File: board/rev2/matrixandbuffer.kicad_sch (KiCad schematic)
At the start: 4 parts, among them J5 Conn_02x08_Counter_Clockwise, SW2 MS-22D28-G020, U15 74HCT245

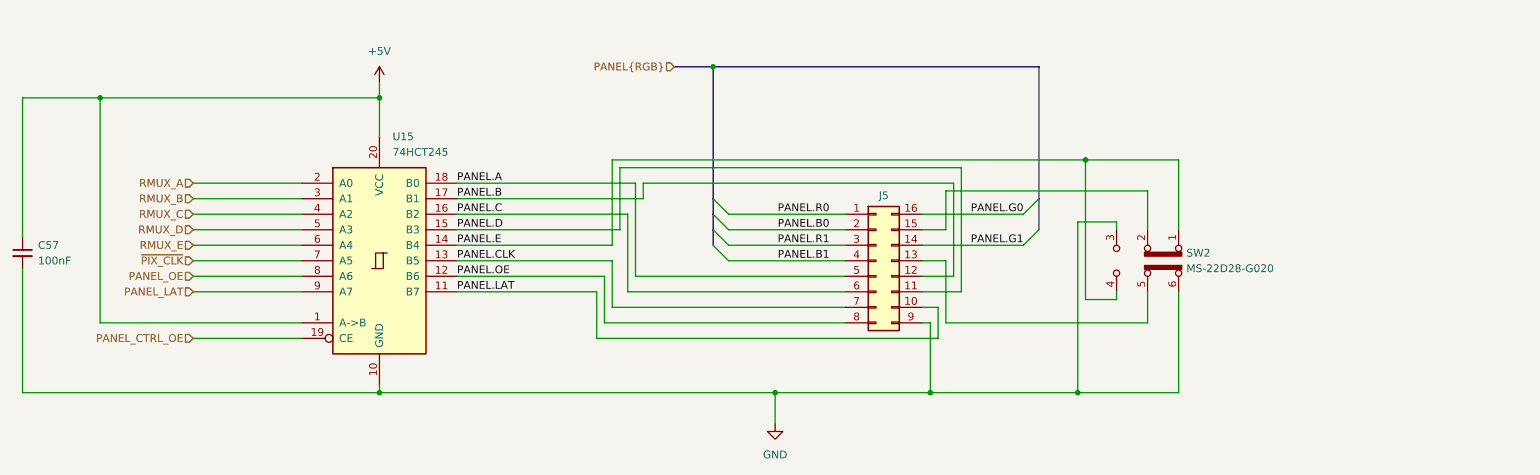
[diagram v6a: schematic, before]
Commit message: Really finish rev2 board schematic
- fix some more footprints
  - move to real SD card holder, for example
- repair part numbers
- add LCSC part refs to everything
- add even more caps to the 3.3V reg output
  - really should use an LDO but meh it should be fine

total BOM cost for 5 of them is apparently 160 CAD, or like 32 dollars
each (don't think that includes the feeder fees tho)
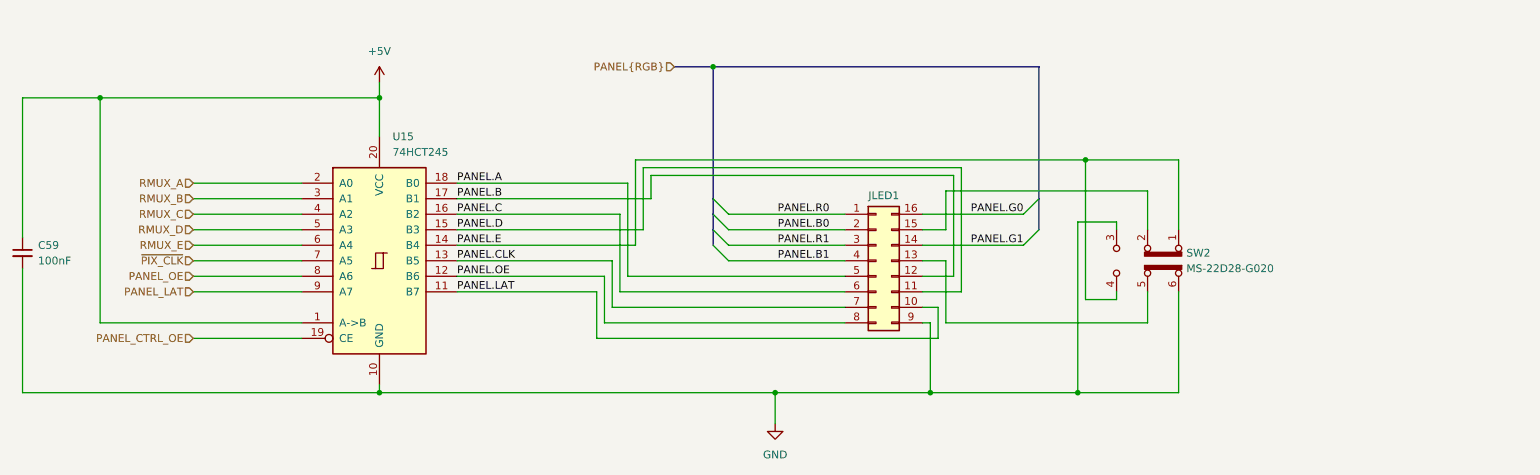
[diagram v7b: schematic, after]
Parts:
- C59: renamed from C57; LCSC (none) -> C307331
- SW2: LCSC (none) -> C963205
- U15: footprint Package_SO:TSSOP-20-1EP_4.4x6.5mm_P0.65mm_EP2.15x3.35mm -> Package_SO:TSSOP-20_4.4x6.5mm_P0.65mm; LCSC (none) -> C5980; Part 74HCT245 -> 74HCT245PW,118
- renumbered J5 to JLED1
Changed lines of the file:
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@@
 	(wire
 		(pts
-			(xy 138.43 91.44) (xy 138.43 104.14)
-		)
-		(stroke
-			(width 0)
-			(type default)
-		)
-	)
-	(wire
-		(pts
-			(xy 110.49 86.36) (xy 139.7 86.36)
+			(xy 137.16 91.44) (xy 137.16 104.14)
+		)
+		(stroke
+			(width 0)
+			(type default)
+		)
+	)
+	(wire
+		(pts
+			(xy 110.49 86.36) (xy 138.43 86.36)
 		)
 		(stroke
@@
 	(wire
 		(pts
-			(xy 139.7 101.6) (xy 173.99 101.6)
-		)
-		(stroke
-			(width 0)
-			(type default)
-		)
-	)
-	(wire
-		(pts
-			(xy 137.16 83.82) (xy 193.04 83.82)
+			(xy 138.43 101.6) (xy 173.99 101.6)
+		)
+		(stroke
+			(width 0)
+			(type default)
+		)
+	)
+	(wire
+		(pts
+			(xy 140.97 83.82) (xy 193.04 83.82)
 		)
 		(stroke
@@
 	(wire
 		(pts
-			(xy 137.16 93.98) (xy 137.16 83.82)
-		)
-		(stroke
-			(width 0)
-			(type default)
-		)
-	)
-	(wire
-		(pts
-			(xy 138.43 104.14) (xy 173.99 104.14)
+			(xy 140.97 93.98) (xy 140.97 83.82)
+		)
+		(stroke
+			(width 0)
+			(type default)
+		)
+	)
+	(wire
+		(pts
+			(xy 137.16 104.14) (xy 173.99 104.14)
 		)
 		(stroke
@@
 	(wire
 		(pts
-			(xy 110.49 93.98) (xy 137.16 93.98)
+			(xy 110.49 93.98) (xy 140.97 93.98)
 		)
 		(stroke
@@
 	(wire
 		(pts
-			(xy 135.89 82.55) (xy 213.36 82.55)
-		)
-		(stroke
-			(width 0)
-			(type default)
-		)
-	)
-	(wire
-		(pts
-			(xy 140.97 88.9) (xy 140.97 86.36)
+			(xy 139.7 82.55) (xy 213.36 82.55)
+		)
+		(stroke
+			(width 0)
+			(type default)
+		)
+	)
+	(wire
+		(pts
+			(xy 142.24 88.9) (xy 142.24 85.09)
 		)
 		(stroke
@@
 	(wire
 		(pts
-			(xy 140.97 86.36) (xy 191.77 86.36)
+			(xy 142.24 85.09) (xy 191.77 85.09)
 		)
 		(stroke
@@
 	(wire
 		(pts
-			(xy 110.49 91.44) (xy 138.43 91.44)
-		)
-		(stroke
-			(width 0)
-			(type default)
-		)
-	)
-	(wire
-		(pts
-			(xy 139.7 86.36) (xy 139.7 101.6)
+			(xy 110.49 91.44) (xy 137.16 91.44)
+		)
+		(stroke
+			(width 0)
+			(type default)
+		)
+	)
+	(wire
+		(pts
+			(xy 138.43 86.36) (xy 138.43 101.6)
 		)
 		(stroke
@@
 	(wire
 		(pts
-			(xy 191.77 86.36) (xy 191.77 101.6)
+			(xy 191.77 85.09) (xy 191.77 101.6)
 		)
 		(stroke
@@
 	(wire
 		(pts
-			(xy 110.49 96.52) (xy 135.89 96.52)
+			(xy 110.49 96.52) (xy 139.7 96.52)
 		)
 		(stroke
@@
 	(wire
 		(pts
-			(xy 135.89 96.52) (xy 135.89 82.55)
+			(xy 139.7 96.52) (xy 139.7 82.55)
 		)
 		(stroke
@@
 	(wire
 		(pts
-			(xy 110.49 88.9) (xy 140.97 88.9)
+			(xy 110.49 88.9) (xy 142.24 88.9)
 		)
 		(stroke
@@
 			)
 		)
-		(property "Footprint" "Package_SO:TSSOP-20-1EP_4.4x6.5mm_P0.65mm_EP2.15x3.35mm"
+		(property "Footprint" "Package_SO:TSSOP-20_4.4x6.5mm_P0.65mm"
 			(at 97.79 99.06 0)
 			(effects
@@
 			)
 		)
-		(property "Part" "74HCT245"
+		(property "Part" "74HCT245PW,118"
+			(at 97.79 99.06 0)
+			(effects
+				(font
+					(size 1.27 1.27)
+				)
+				(hide yes)
+			)
+		)
+		(property "LCSC" "C5980"
 			(at 97.79 99.06 0)
 			(effects
@@
 		(dnp no)
 		(fields_autoplaced yes)
-		(property "Reference" "C57"
+		(property "Reference" "C59"
 			(at 41.91 96.5262 0)
 			(effects
@@
 		)
 		(property "Part" "CL05B104KB54PNC"
+			(at 39.37 97.79 0)
+			(effects
+				(font
+					(size 1.27 1.27)
+				)
+				(hide yes)
+			)
+		)
+		(property "LCSC" "C307331 "
 			(at 39.37 97.79 0)
 			(effects
@@
 			(project "mainboard"
 				(path "/32eb05c7-b4a6-42f3-8fb3-43453631100f/b5a611d3-6308-4792-ad5f-d479afbae4ce"
-					(reference "C57")
+					(reference "C59")
 					(unit 1)
 				)
 				(path "/32eb05c7-b4a6-42f3-8fb3-43453631100f/e7e17249-2796-40aa-8cf6-7a1737723276"
-					(reference "C58")
+					(reference "C60")
 					(unit 1)
 				)
@@
 		(dnp no)
 		(fields_autoplaced yes)
-		(property "Reference" "#PWR045"
+		(property "Reference" "#PWR046"
 			(at 97.79 73.66 0)
 			(effects
@@
 			(project "mainboard"
 				(path "/32eb05c7-b4a6-42f3-8fb3-43453631100f/b5a611d3-6308-4792-ad5f-d479afbae4ce"
-					(reference "#PWR045")
+					(reference "#PWR046")
 					(unit 1)
 				)
 				(path "/32eb05c7-b4a6-42f3-8fb3-43453631100f/e7e17249-2796-40aa-8cf6-7a1737723276"
-					(reference "#PWR047")
+					(reference "#PWR048")
 					(unit 1)
 				)
@@
 			)
 		)
+		(property "LCSC" "C963205"
+			(at 223.52 99.06 90)
+			(effects
+				(font
+					(size 1.27 1.27)
+				)
+				(hide yes)
+			)
+		)
 		(pin "5"
 		)
@@
 		(on_board yes)
 		(dnp no)
-		(property "Reference" "J5"
+		(property "Reference" "JLED1"
 			(at 180.34 88.392 0)
 			(effects
@@
 					(size 1.27 1.27)
 					(color 255 255 194 1)
+				)
+				(hide yes)
+			)
+		)
+		(property "LCSC" ""
+			(at 179.07 99.06 0)
+			(effects
+				(font
+					(size 1.27 1.27)
 				)
 				(hide yes)
@@
 			(project "mainboard"
 				(path "/32eb05c7-b4a6-42f3-8fb3-43453631100f/b5a611d3-6308-4792-ad5f-d479afbae4ce"
-					(reference "J5")
+					(reference "JLED1")
 					(unit 1)
 				)
 				(path "/32eb05c7-b4a6-42f3-8fb3-43453631100f/e7e17249-2796-40aa-8cf6-7a1737723276"
-					(reference "J6")
+					(reference "JLED2")
 					(unit 1)
 				)
@@
 		(dnp no)
 		(fields_autoplaced yes)
-		(property "Reference" "#PWR046"
+		(property "Reference" "#PWR047"
 			(at 162.56 132.08 0)
 			(effects
@@
 			(project "mainboard"
 				(path "/32eb05c7-b4a6-42f3-8fb3-43453631100f/b5a611d3-6308-4792-ad5f-d479afbae4ce"
-					(reference "#PWR046")
+					(reference "#PWR047")
 					(unit 1)
 				)
 				(path "/32eb05c7-b4a6-42f3-8fb3-43453631100f/e7e17249-2796-40aa-8cf6-7a1737723276"
-					(reference "#PWR048")
+					(reference "#PWR049")
 					(unit 1)
 				)

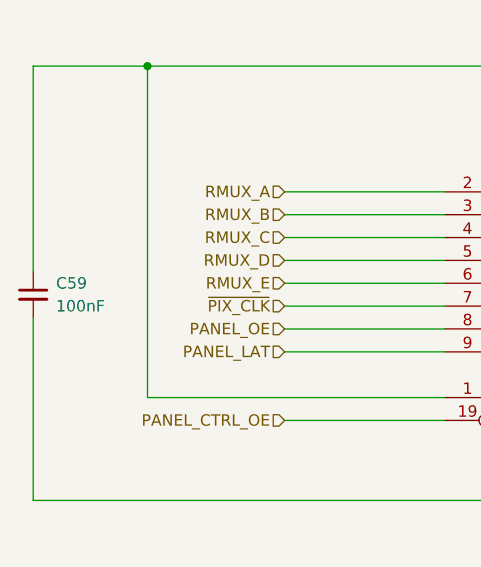
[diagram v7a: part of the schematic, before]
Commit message: Start board
add a few extra bypass caps too, and swap some pins on the USB mux

i forgot to add a bypass cap on the tpd6s so that also needs to happen

truly 63 capacitors is not enough
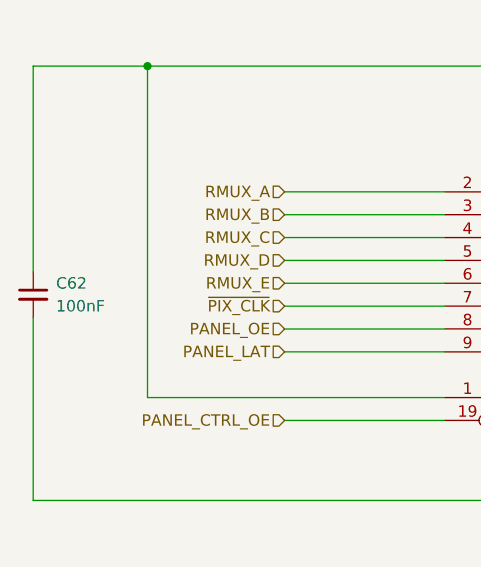
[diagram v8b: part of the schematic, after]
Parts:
- renumbered C59 to C62
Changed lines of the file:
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@@
 		(dnp no)
 		(fields_autoplaced yes)
-		(property "Reference" "C59"
+		(property "Reference" "C62"
 			(at 41.91 96.5262 0)
 			(effects
@@
 			(project "mainboard"
 				(path "/32eb05c7-b4a6-42f3-8fb3-43453631100f/b5a611d3-6308-4792-ad5f-d479afbae4ce"
-					(reference "C59")
+					(reference "C62")
 					(unit 1)
 				)
 				(path "/32eb05c7-b4a6-42f3-8fb3-43453631100f/e7e17249-2796-40aa-8cf6-7a1737723276"
-					(reference "C60")
+					(reference "C63")
 					(unit 1)
 				)
@@
 		(dnp no)
 		(fields_autoplaced yes)
-		(property "Reference" "#PWR046"
+		(property "Reference" "#PWR047"
 			(at 97.79 73.66 0)
 			(effects
@@
 			(project "mainboard"
 				(path "/32eb05c7-b4a6-42f3-8fb3-43453631100f/b5a611d3-6308-4792-ad5f-d479afbae4ce"
-					(reference "#PWR046")
+					(reference "#PWR047")
 					(unit 1)
 				)
 				(path "/32eb05c7-b4a6-42f3-8fb3-43453631100f/e7e17249-2796-40aa-8cf6-7a1737723276"
-					(reference "#PWR048")
+					(reference "#PWR049")
 					(unit 1)
 				)
@@
 		(dnp no)
 		(fields_autoplaced yes)
-		(property "Reference" "#PWR047"
+		(property "Reference" "#PWR048"
 			(at 162.56 132.08 0)
 			(effects
@@
 			(project "mainboard"
 				(path "/32eb05c7-b4a6-42f3-8fb3-43453631100f/b5a611d3-6308-4792-ad5f-d479afbae4ce"
-					(reference "#PWR047")
+					(reference "#PWR048")
 					(unit 1)
 				)
 				(path "/32eb05c7-b4a6-42f3-8fb3-43453631100f/e7e17249-2796-40aa-8cf6-7a1737723276"
-					(reference "#PWR049")
-					(unit 1)
-				)
+					(reference "#PWR050")
+					(unit 1)
+				)
